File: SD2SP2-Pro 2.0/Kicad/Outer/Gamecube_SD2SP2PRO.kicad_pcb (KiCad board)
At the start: 2 copper layers, 36.5 x 46.3 mm, 4 parts, among them J2 Conn_02x04_Odd_Even, J3 Micro_SD_Card, U1 74AHC1G32

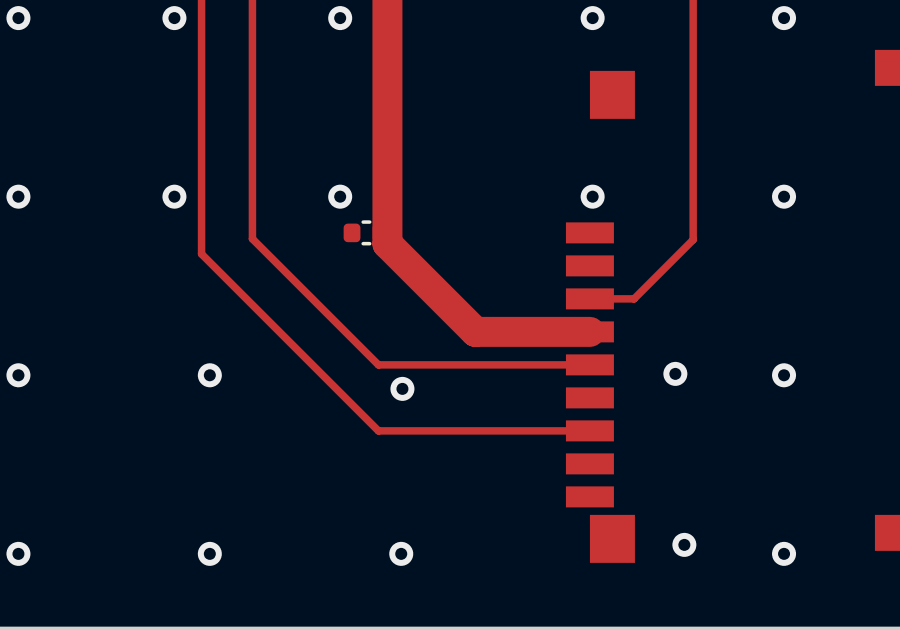
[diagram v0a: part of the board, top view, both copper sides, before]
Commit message: Outer Board C1 Silkscreen and relocation
Moved C1 closer to MicroSD slot and fixed C1 Silkscreen layer
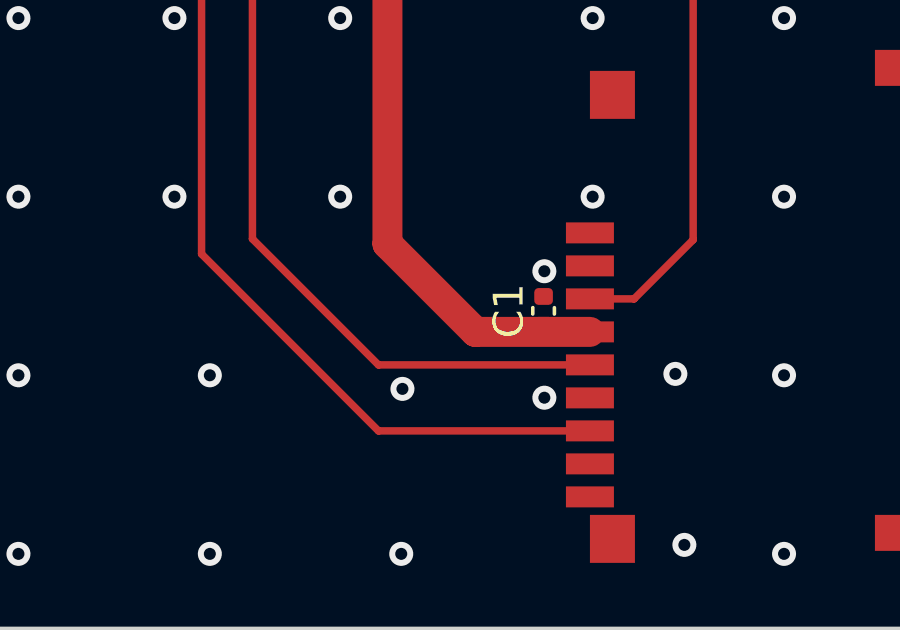
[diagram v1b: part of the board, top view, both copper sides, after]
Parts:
- C1: value 100n -> 22u
- moved C1 6.45 mm to (94.0, 90.4), turned to 90 degrees
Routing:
- net GND: vias 45 -> 47
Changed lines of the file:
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@@
 	(footprint "Capacitor_SMD:C_0402_1005Metric"
 		(layer "F.Cu")
-		(at 88.1 87.8 180)
+		(at 94.0054 90.3986 90)
 		(descr "Capacitor SMD 0402 (1005 Metric), square (rectangular) end terminal, IPC_7351 nominal, (Body size source: IPC-SM-782 page 76, https://www.pcb-3d.com/wordpress/wp-content/uploads/ipc-sm-782a_amendment_1_and_2.pdf), generated with kicad-footprint-generator")
 		(tags "capacitor")
 		(property "Reference" "C1"
-			(at 0 -1.16 0)
-			(layer "F.Fab")
+			(at 0 -1.16 90)
+			(layer "F.SilkS")
 			(effects
 				(font
@@
 			)
 		)
-		(property "Value" "100n"
-			(at 0 1.16 0)
+		(property "Value" "22u"
+			(at 0 1.16 90)
 			(layer "F.Fab")
 			(effects
@@
 		)
 		(property "Footprint" "Capacitor_SMD:C_0402_1005Metric"
-			(at 0 0 180)
+			(at 0 0 90)
 			(layer "F.Fab")
 			(hide yes)
@@
 		)
 		(property "Datasheet" ""
-			(at 0 0 180)
+			(at 0 0 90)
 			(layer "F.Fab")
 			(hide yes)
@@
 		)
 		(property "Description" ""
-			(at 0 0 180)
+			(at 0 0 90)
 			(layer "F.Fab")
 			(hide yes)
@@
 		)
 		(property "LCSC Part" "C1525"
-			(at 176.2 175.6 0)
+			(at 176.2 175.6 90)
 			(layer "F.Fab")
 			(hide yes)
@@
 		(attr smd)
 		(fp_line
+			(start -0.107836 -0.36)
+			(end 0.107836 -0.36)
+			(stroke
+				(width 0.12)
+				(type solid)
+			)
+			(layer "F.SilkS")
+		)
+		(fp_line
 			(start -0.107836 0.36)
 			(end 0.107836 0.36)
@@
 		)
 		(fp_line
-			(start -0.107836 -0.36)
-			(end 0.107836 -0.36)
-			(stroke
-				(width 0.12)
-				(type solid)
-			)
-			(layer "F.SilkS")
+			(start 0.91 -0.46)
+			(end 0.91 0.46)
+			(stroke
+				(width 0.05)
+				(type solid)
+			)
+			(layer "F.CrtYd")
+		)
+		(fp_line
+			(start -0.91 -0.46)
+			(end 0.91 -0.46)
+			(stroke
+				(width 0.05)
+				(type solid)
+			)
+			(layer "F.CrtYd")
 		)
 		(fp_line
@@
 		)
 		(fp_line
-			(start 0.91 -0.46)
-			(end 0.91 0.46)
-			(stroke
-				(width 0.05)
-				(type solid)
-			)
-			(layer "F.CrtYd")
-		)
-		(fp_line
 			(start -0.91 0.46)
 			(end -0.91 -0.46)
@@
 		)
 		(fp_line
-			(start -0.91 -0.46)
-			(end 0.91 -0.46)
-			(stroke
-				(width 0.05)
-				(type solid)
-			)
-			(layer "F.CrtYd")
+			(start 0.5 -0.25)
+			(end 0.5 0.25)
+			(stroke
+				(width 0.1)
+				(type solid)
+			)
+			(layer "F.Fab")
+		)
+		(fp_line
+			(start -0.5 -0.25)
+			(end 0.5 -0.25)
+			(stroke
+				(width 0.1)
+				(type solid)
+			)
+			(layer "F.Fab")
 		)
 		(fp_line
@@
 		)
 		(fp_line
-			(start 0.5 -0.25)
-			(end 0.5 0.25)
-			(stroke
-				(width 0.1)
-				(type solid)
-			)
-			(layer "F.Fab")
-		)
-		(fp_line
 			(start -0.5 0.25)
 			(end -0.5 -0.25)
@@
 			(layer "F.Fab")
 		)
-		(fp_line
-			(start -0.5 -0.25)
-			(end 0.5 -0.25)
-			(stroke
-				(width 0.1)
-				(type solid)
-			)
-			(layer "F.Fab")
-		)
 		(fp_text user "${REFERENCE}"
-			(at 0 0 0)
+			(at 0 0 90)
 			(layer "F.Fab")
 			(effects
@@
 		)
 		(pad "1" smd roundrect
-			(at -0.48 0 180)
+			(at -0.48 0 90)
 			(size 0.56 0.62)
 			(layers "F.Cu" "F.Paste" "F.Mask")
@@
 		)
 		(pad "2" smd roundrect
-			(at 0.48 0 180)
+			(at 0.48 0 90)
 			(size 0.56 0.62)
 			(layers "F.Cu" "F.Paste" "F.Mask")
@@
 	)
 	(via
+		(at 94.0308 89.0778)
+		(size 0.8)
+		(drill 0.4)
+		(layers "F.Cu" "B.Cu")
+		(free yes)
+		(net 2)
+	)
+	(via
 		(at 102.02 86.593247)
 		(size 0.8)
@@
 		(size 0.8)
 		(drill 0.4)
+		(layers "F.Cu" "B.Cu")
+		(free yes)
+		(net 2)
+	)
+	(via
+		(at 94.0308 93.2942)
+		(size 0.8)
+		(drill 0.4)
